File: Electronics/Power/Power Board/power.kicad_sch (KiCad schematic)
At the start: 119 parts, among them IC202 TLV1805DBVR, IC205 MP28167GQ-A-Z, IC206 TPS563202DRLR, IC207 TPS563202DRLR, IC208 TLV1805DBVR, IC3 INA219AIDR, J10 Conn_01x02_Pin, J11 Conn_01x02_Pin, J2 Screw_Terminal_01x02, J201 XT60PW-F, J203 XT60PW-M, J9 Conn_01x02_Pin, Q201 DMP3013SFV-7, Q202 DMP3013SFV-7, Q203 DMP3013SFV-7, Q204 DMP3013SFV-7, Q205 DMP3013SFV-7, Q206 SSM6K513NU,LF, Q207 SSM6K513NU,LF, SW201 SW_SPDT, U201 TCKE800NA_RF, U202 TCKE812NA_RF, U304 TVS1800DRV

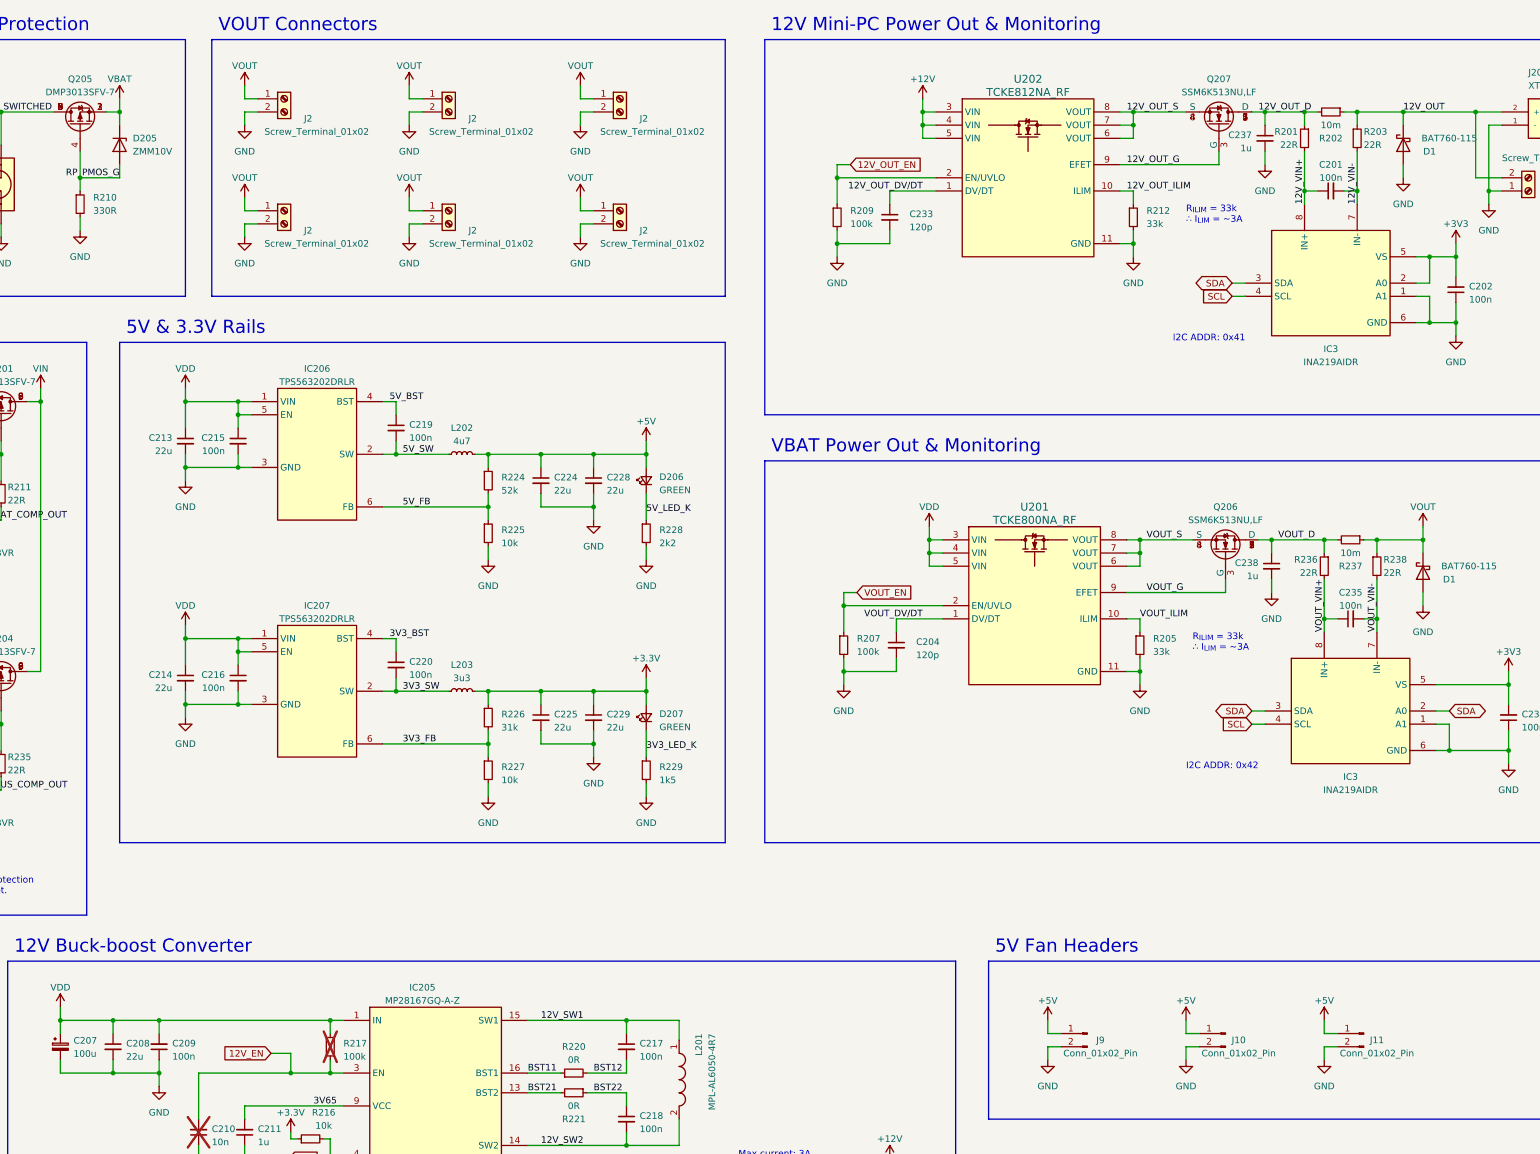
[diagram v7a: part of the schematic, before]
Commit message: Gateway board layout complete and routing begun
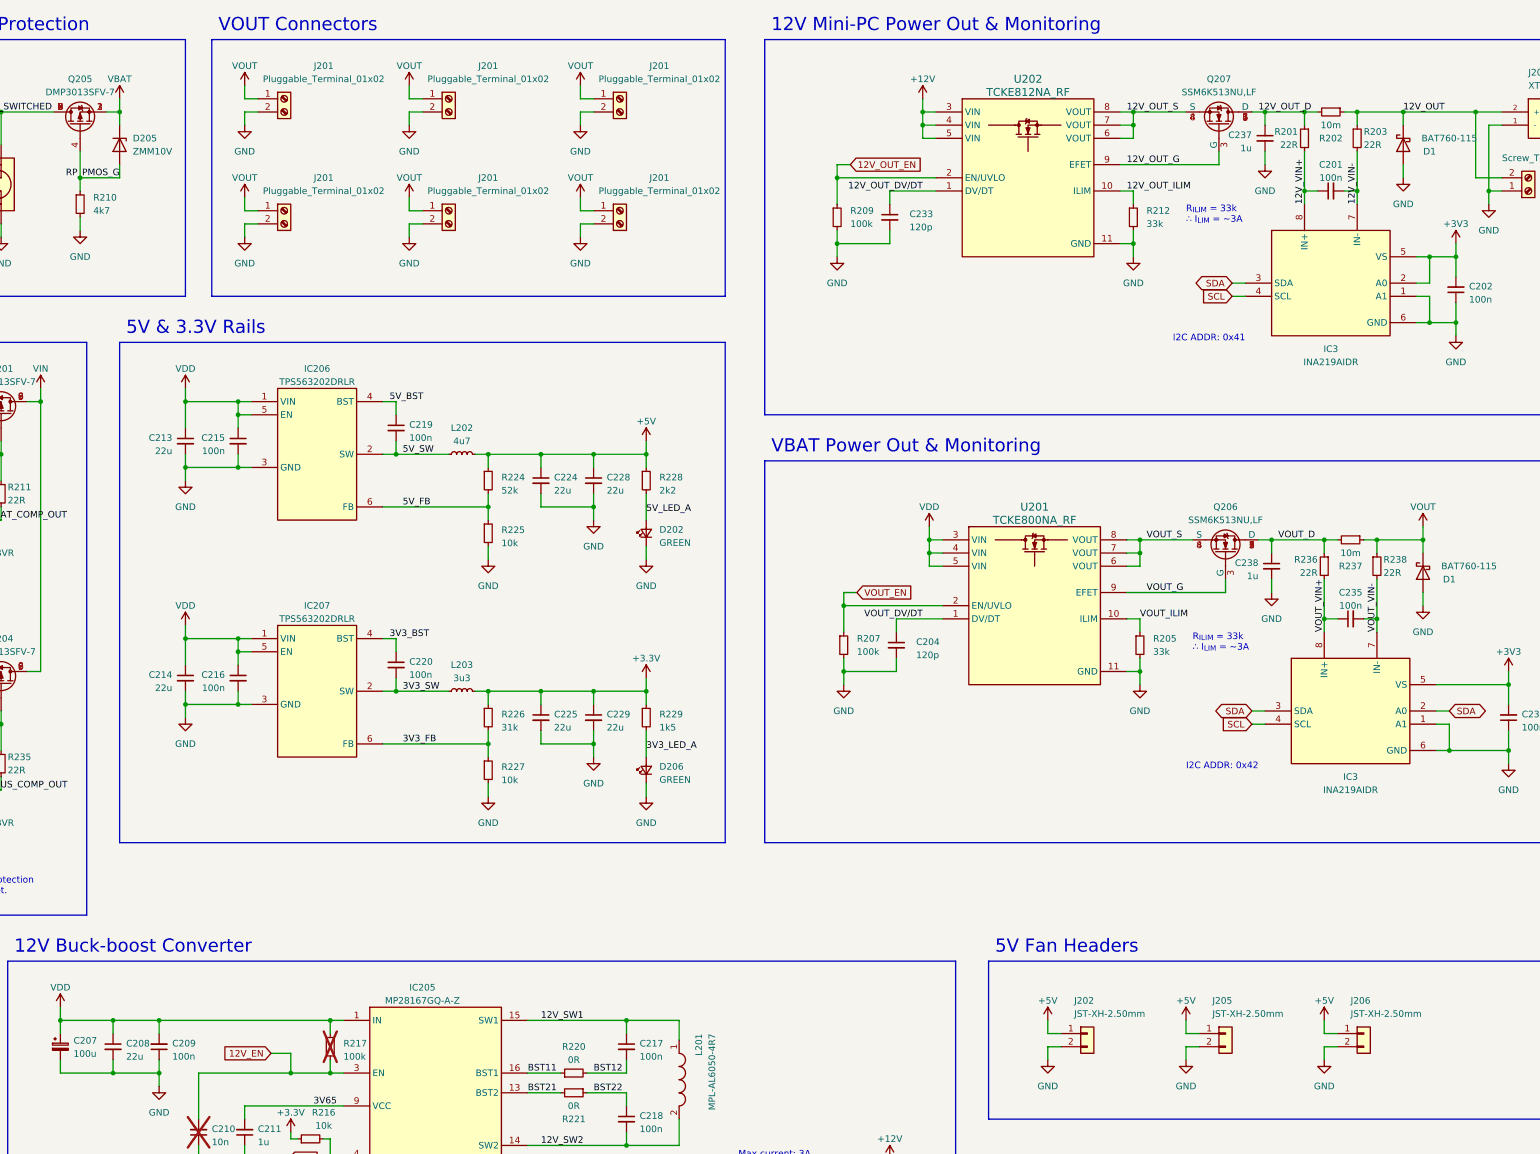
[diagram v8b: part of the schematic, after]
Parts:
- removed D207: GREEN, LED_SMD:LED_0603_1608Metric, symbol Device:LED_Small
- removed J10, J11, J9: Conn_01x02_Pin, Connector_PinHeader_2.54mm:PinHeader_1x02_P2.54mm_Vertical, symbol Connector:Conn_01x02_Pin
- removed J2 (x6): Screw_Terminal_01x02, TerminalBlock:TerminalBlock_bornier-2_P5.08mm, symbol Connector:Screw_Terminal_01x02
- added D202: GREEN, LED_SMD:LED_0603_1608Metric, symbol Device:LED_Small
- added J201 (x6): Pluggable_Terminal_01x02, MSL Footprints:Pluggable_terminal-2_P5.08mm, symbol MSL_Symbols:Pluggable_Terminal_01x02
- added J202, J205, J206: JST-XH-2.50mm, Connector_JST:JST_XH_B2B-XH-A_1x02_P2.50mm_Vertical, symbol MSL_Symbols:JST_2.5mm_1x2
- R210: value 330R -> 4k7
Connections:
- net 3V3_LED_K is gone; now on net +3.3V: R229.1
- net +5V: now also R228.1, J202.1 (Pin_1), J205.1 (Pin_1), J206.1 (Pin_1); no longer D206.2 (A)
- net GND: now also D206.1 (K), D202.1 (K), J201.2 (Pin_2), J201.2 (Pin_2), J201.2 (Pin_2), J201.2 (Pin_2), J201.2 (Pin_2), J201.2 (Pin_2), J202.2 (Pin_2), J205.2 (Pin_2), J206.2 (Pin_2); no longer R228.2, R229.2
- net VOUT: now also J201.1 (Pin_1), J201.1 (Pin_1), J201.1 (Pin_1), J201.1 (Pin_1), J201.1 (Pin_1), J201.1 (Pin_1)
- removed net 5V_LED_K: D206.1 (K), R228.1
- new net 3V3_LED_A: D206.2 (A), R229.2
- new net 5V_LED_A: D202.2 (A), R228.2
